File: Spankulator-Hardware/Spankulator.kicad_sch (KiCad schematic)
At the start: 106 parts, among them J1 3.5mm Jack, J12 Arduino Socket, J13 Arduino Socket, J2 2x5 Header, J3 3.5mm Jack, J4 3.5mm Jack, J5 3.5mm Jack, J6 3.5mm Jack, J7 2x5 Header, J9 Display Header, Q1 2N3904, Q2 VP2106/ZVP3306A, Q3 2N7000, Q4 VP2106/ZVP3306A, Q5 2N7000, Q7 2N7000, Q8 2N7000, SW1 Adj, SW2 Push Button, SW3 Push Button, SW4 Push Button, SW5 Push Button, SW6 Push Button, SW7 Push Button, SW8 Push Button, U1 TL072CP, U2 CD4013BE, U3 TL072CP, U4 MC78L05_TO92, U5 LP2950-3.3_TO92, U6 MAX7480, U7 MB85RC256

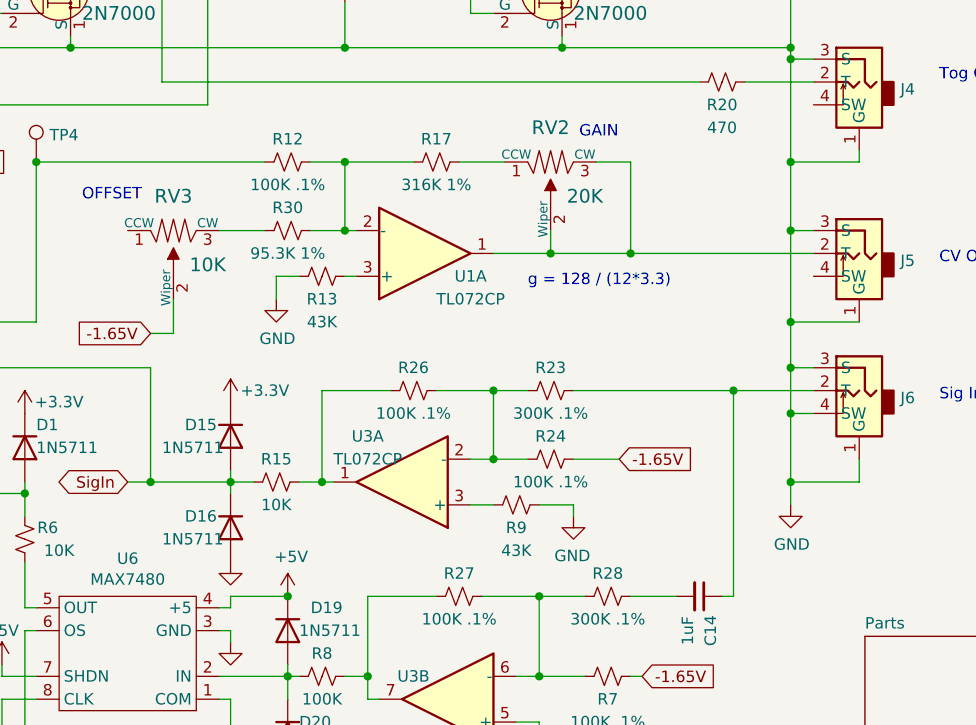
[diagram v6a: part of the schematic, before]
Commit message: Upgrade board to 5.1
Changes to DAC output components.
Improvements to silkscreen.
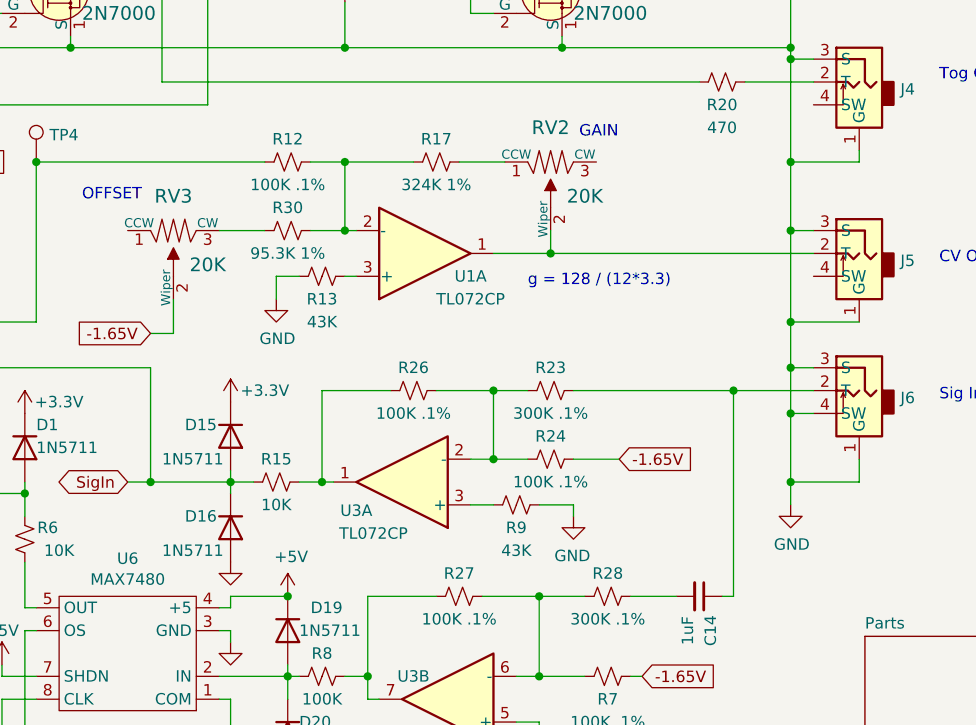
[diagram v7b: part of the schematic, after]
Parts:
- R17: value 316K 1% -> 324K 1%; Digi-Key Part 316KXBK-ND -> 324KXBK-ND; LCSC Part # C172901 -> C1369146
- RV3: value 10K -> 20K; Digi-Key Part 490-2875-ND -> 490-2881-ND; URL (none) -> https://www.amazon.com/dp/B015RK03LI?psc=1&ref=ppx_yo2ov_dt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
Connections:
- net at J5.2 (T), RV2.2 (Wiper), U1.1: no longer RV2.3 (CW)
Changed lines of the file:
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@@
   (title_block
     (title "Spankulator")
-    (rev "5.0")
+    (rev "5.1")
     (company "Greenface Labs")
   )
@@
   (junction (at 158.75 184.15) (diameter 0) (color 0 0 0 0)
   )
-  (junction (at 229.87 66.04) (diameter 0) (color 0 0 0 0)
-  )
   (junction (at 193.675 156.21) (diameter 0) (color 0 0 0 0)
   )
@@
     (stroke (width 0) (type default) (color 0 0 0 0))
   )
-  (wire (pts (xy 229.87 55.88) (xy 229.87 66.04))
-    (stroke (width 0) (type default) (color 0 0 0 0))
-  )
   (wire (pts (xy 176.53 74.93) (xy 179.07 74.93))
     (stroke (width 0) (type default) (color 0 0 0 0))
@@
     (stroke (width 0) (type default) (color 0 0 0 0))
   )
-  (wire (pts (xy 220.98 66.04) (xy 229.87 66.04))
+  (wire (pts (xy 220.98 66.04) (xy 250.19 66.04))
     (stroke (width 0) (type default) (color 0 0 0 0))
   )
@@
     (stroke (width 0) (type default) (color 0 0 0 0))
   )
-  (wire (pts (xy 226.06 55.88) (xy 229.87 55.88))
-    (stroke (width 0) (type default) (color 0 0 0 0))
-  )
-  (wire (pts (xy 229.87 66.04) (xy 250.19 66.04))
-    (stroke (width 0) (type default) (color 0 0 0 0))
-  )
   (wire (pts (xy 222.25 17.78) (xy 222.25 13.97))
     (stroke (width 0) (type default) (color 0 0 0 0))
@@
   (symbol (lib_id "Amplifier_Operational:TL072") (at 204.47 91.44 180) (unit 1)
     (in_bom yes) (on_board yes)
-    (property "Reference" "U3" (id 0) (at 200.66 86.36 0))
-    (property "Value" "TL072CP" (id 1) (at 200.66 88.9 0))
+    (property "Reference" "U3" (id 0) (at 199.39 94.615 0))
+    (property "Value" "TL072CP" (id 1) (at 201.295 97.155 0))
     (property "Footprint" "Package_DIP:DIP-8_W7.62mm_Socket" (id 2) (at 205.74 93.98 0)
       (effects (font (size 1.27 1.27)) hide)
@@
     (in_bom yes) (on_board yes)
     (property "Reference" "R17" (id 0) (at 208.28 53.34 90))
-    (property "Value" "316K 1%" (id 1) (at 208.28 58.42 90))
+    (property "Value" "324K 1%" (id 1) (at 208.28 58.42 90))
     (property "Footprint" "Resistor_THT:R_Axial_DIN0207_L6.3mm_D2.5mm_P10.16mm_Horizontal" (id 2) (at 208.28 55.88 0)
       (effects (font (size 1.27 1.27)) hide)
@@
       (effects (font (size 1.27 1.27)) hide)
     )
-    (property "Digi-Key Part" "316KXBK-ND" (id 4) (at 208.28 55.88 90)
+    (property "Digi-Key Part" "324KXBK-ND" (id 4) (at 208.28 55.88 90)
       (effects (font (size 1.27 1.27)) hide)
     )
-    (property "LCSC Part #" "C172901" (id 5) (at 208.28 55.88 0)
+    (property "LCSC Part #" "C1369146" (id 5) (at 208.28 55.88 0)
       (effects (font (size 1.27 1.27)) hide)
     )
@@
       (effects (font (size 1.524 1.524)))
     )
-    (property "Value" "10K" (id 1) (at 182.88 67.31 0)
+    (property "Value" "20K" (id 1) (at 182.88 67.31 0)
       (effects (font (size 1.524 1.524)))
     )
@@
       (effects (font (size 1.524 1.524)) (justify left) hide)
     )
-    (property "Digi-Key Part" "490-2875-ND" (id 4) (at 184.15 73.66 0)
+    (property "Digi-Key Part" "490-2881-ND" (id 4) (at 184.15 73.66 0)
       (effects (font (size 1.524 1.524)) (justify left) hide)
     )
+    (property "URL" "https://www.amazon.com/dp/B015RK03LI?psc=1&ref=ppx_yo2ov_dt_b_product_details" (id 5) (at 179.07 63.5 0)
+      (effects (font (size 1.27 1.27)) hide)
+    )
     (pin "1")
     (pin "2")
@@
       (effects (font (size 1.27 1.27)) (justify left))
     )
-    (property "Value" "1N5711" (id 1) (at 177.8 97.79 90)
+    (property "Value" "1N5711" (id 1) (at 177.8 99.06 90)
       (effects (font (size 1.27 1.27)) (justify left))
     )
@@
       (effects (font (size 1.27 1.27)) (justify left))
     )
-    (property "Value" "1N5711" (id 1) (at 177.8 87.63 90)
+    (property "Value" "1N5711" (id 1) (at 177.8 88.9 90)
       (effects (font (size 1.27 1.27)) (justify left))
     )
@@
       (reference "J9") (unit 1) (value "Display Header") (footprint "sputterizer:OLED_Header_Slim")
     )
-    (path "/681cdba4-7e5c-45e3-bb80-441c833d63d5/25329de1-aee4-4830-8b44-b75dc790f729"
-      (reference "J10") (unit 1) (value "FRAM Pins") (footprint "")
-    )
     (path "/681cdba4-7e5c-45e3-bb80-441c833d63d5/b50e328b-5b8d-4db0-8879-b2afd5ea155d"
       (reference "J11") (unit 1) (value "OLED Pins") (footprint "")
@@
       (reference "KN2") (unit 1) (value "CV Knob") (footprint "")
     )
-    (path "/681cdba4-7e5c-45e3-bb80-441c833d63d5/78ea5144-b99a-468b-96b1-53a437c9146d"
-      (reference "M1") (unit 1) (value "FRAM_Module") (footprint "")
-    )
     (path "/681cdba4-7e5c-45e3-bb80-441c833d63d5/e98410a5-9264-4ef1-b085-4536153ea768"
       (reference "M2") (unit 1) (value "OLED") (footprint "")
     )
-    (path "/681cdba4-7e5c-45e3-bb80-441c833d63d5/b2d7e3ce-20a7-4f6b-9f2d-a0ac35d9d422"
-      (reference "N1") (unit 1) (value "Nut") (footprint "")
-    )
     (path "/681cdba4-7e5c-45e3-bb80-441c833d63d5/328128c5-242b-4af1-a65c-2d865cf59cf4"
       (reference "N2") (unit 1) (value "Nut") (footprint "")
@@
     )
     (path "/00000000-0000-0000-0000-00005f427c66"
-      (reference "R17") (unit 1) (value "316K 1%") (footprint "Resistor_THT:R_Axial_DIN0207_L6.3mm_D2.5mm_P10.16mm_Horizontal")
+      (reference "R17") (unit 1) (value "324K 1%") (footprint "Resistor_THT:R_Axial_DIN0207_L6.3mm_D2.5mm_P10.16mm_Horizontal")
     )
     (path "/00000000-0000-0000-0000-000061fe5406"
@@
     )
     (path "/00000000-0000-0000-0000-000060e1c67d"
-      (reference "RV3") (unit 1) (value "10K") (footprint "Potentiometer_THT:Potentiometer_Bourns_3266Y_Vertical")
-    )
-    (path "/681cdba4-7e5c-45e3-bb80-441c833d63d5/ca43a104-c67e-44de-a354-46d47513b5fa"
-      (reference "SC1") (unit 1) (value "Nylon Screw") (footprint "")
+      (reference "RV3") (unit 1) (value "20K") (footprint "Potentiometer_THT:Potentiometer_Bourns_3266Y_Vertical")
     )
     (path "/681cdba4-7e5c-45e3-bb80-441c833d63d5/7b7e213f-86ba-46e4-a2d6-48bd276133ca"
@@
       (reference "SK4") (unit 1) (value "A_14-LC-TT") (footprint "")
     )
-    (path "/681cdba4-7e5c-45e3-bb80-441c833d63d5/86c0b3a9-57b5-4585-8c86-327bdede09fe"
-      (reference "SO1") (unit 1) (value "Standoff 7mm") (footprint "")
-    )
     (path "/681cdba4-7e5c-45e3-bb80-441c833d63d5/6714bf9c-71a2-48ee-b6d1-afbf0097602e"

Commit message: Corrects 3904 part number
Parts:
- Q1: LCSC Part # C94514 -> C258185
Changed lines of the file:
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@@
       (effects (font (size 1.27 1.27)) hide)
     )
-    (property "LCSC Part #" "C94514" (id 6) (at 124.46 142.24 0)
+    (property "LCSC Part #" "C258185" (id 6) (at 124.46 142.24 0)
       (effects (font (size 1.27 1.27)) hide)
     )
